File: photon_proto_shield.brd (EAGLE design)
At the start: 35.6 x 35.6 mm, 15 parts

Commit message: update
changed name on silk
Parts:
- added LOGO1: SFE_LOGO_NAME.1_INCH, SparkFun-Aesthetics:SFE_LOGO_NAME_.1
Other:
- board text added: "PROTO SHIELD FOR PHOTON"
- board text removed: "PHOTON PROTO SHIELD"
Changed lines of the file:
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@@
 <layer number="47" name="Measures" color="7" fill="1" visible="no" active="yes"/>
 <layer number="48" name="Document" color="7" fill="1" visible="no" active="yes"/>
-<layer number="49" name="Reference" color="7" fill="1" visible="yes" active="yes"/>
+<layer number="49" name="Reference" color="7" fill="1" visible="no" active="yes"/>
 <layer number="50" name="dxf" color="7" fill="1" visible="no" active="no"/>
 <layer number="51" name="tDocu" color="6" fill="1" visible="yes" active="yes"/>
@@
 <wire x1="33.02" y1="0" x2="2.54" y2="0" width="0.2032" layer="20"/>
 <wire x1="2.54" y1="0" x2="0" y2="2.54" width="0.2032" layer="20" curve="-90"/>
-<text x="35.052" y="6.858" size="1.143" layer="21" font="vector" ratio="15" rot="R90">PHOTON PROTO SHIELD</text>
+<text x="34.925" y="4.826" size="1.016" layer="21" font="vector" ratio="15" rot="R90">PROTO SHIELD FOR PHOTON</text>
 <text x="15.494" y="32.004" size="0.8128" layer="21" font="vector" ratio="15">3V3</text>
 <text x="18.161" y="32.004" size="0.8128" layer="21" font="vector" ratio="15">SDA</text>
@@
 <dimension x1="0" y1="0" x2="0" y2="35.56" x3="-7.62" y3="17.78" textsize="0.8128" textratio="15" layer="47" unit="inch"/>
 <dimension x1="35.56" y1="35.56" x2="30.734" y2="33.02" x3="33.147" y3="36.83" textsize="0.8128" textratio="15" layer="47" dtype="horizontal" unit="inch"/>
-<text x="33.909" y="6.858" size="1.143" layer="22" font="vector" ratio="15" rot="MR90">PHOTON PROTO SHIELD</text>
+<text x="33.909" y="4.826" size="1.016" layer="22" font="vector" ratio="15" rot="MR90">PROTO SHIELD FOR PHOTON</text>
 <text x="15.113" y="27.94" size="1.016" layer="22" font="vector" ratio="15" rot="MR0">GND</text>
 <text x="22.86" y="27.94" size="1.016" layer="22" font="vector" ratio="15" rot="MR0">3V3</text>
@@
 <element name="JP9" library="SparkFun-Connectors" package="1X09_NO_SILK" value="" x="21.59" y="6.35" rot="R90"/>
 <element name="JP10" library="SparkFun-Connectors" package="1X09_NO_SILK" value="" x="24.13" y="6.35" rot="R90"/>
+<element name="LOGO1" library="SparkFun-Aesthetics" package="SFE_LOGO_NAME_.1" value="SFE_LOGO_NAME.1_INCH" x="0" y="5.461" rot="MR90"/>
 </elements>
 <signals>

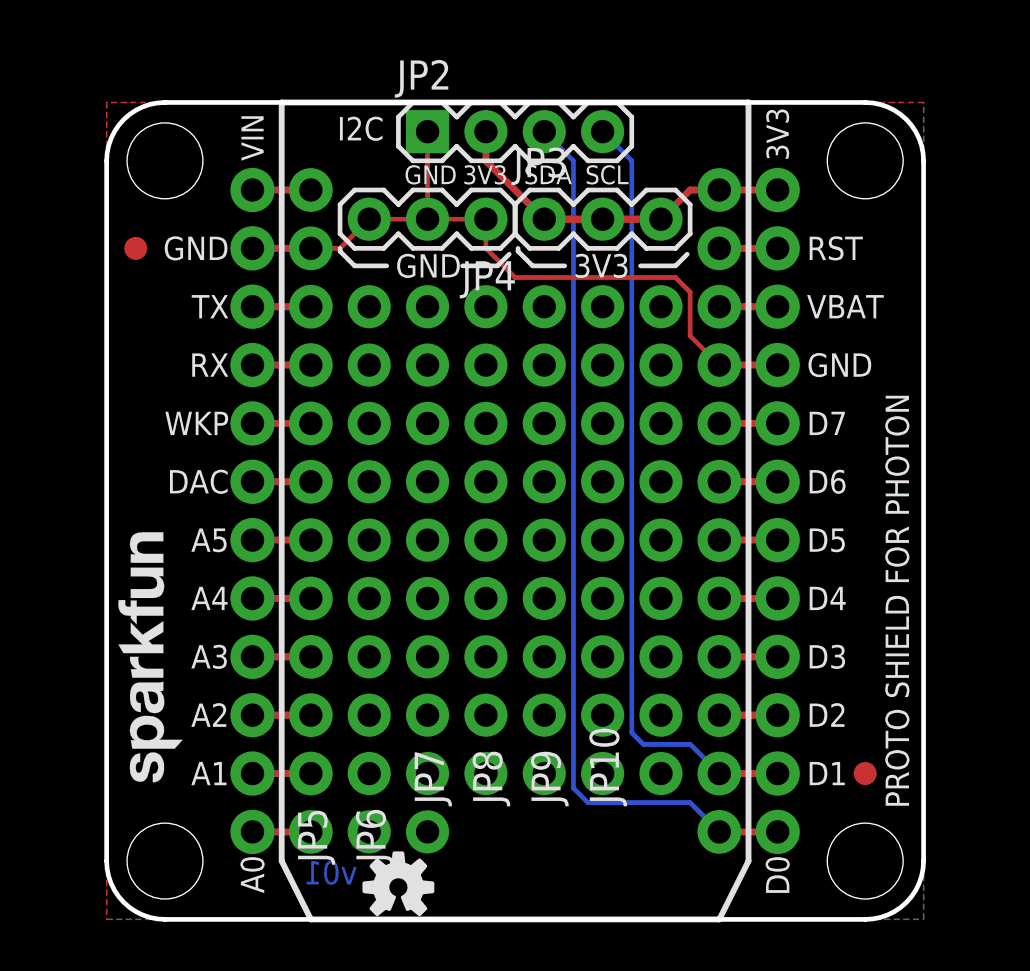
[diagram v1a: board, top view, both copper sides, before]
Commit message: Adding gap between Photon and pin breakouts.
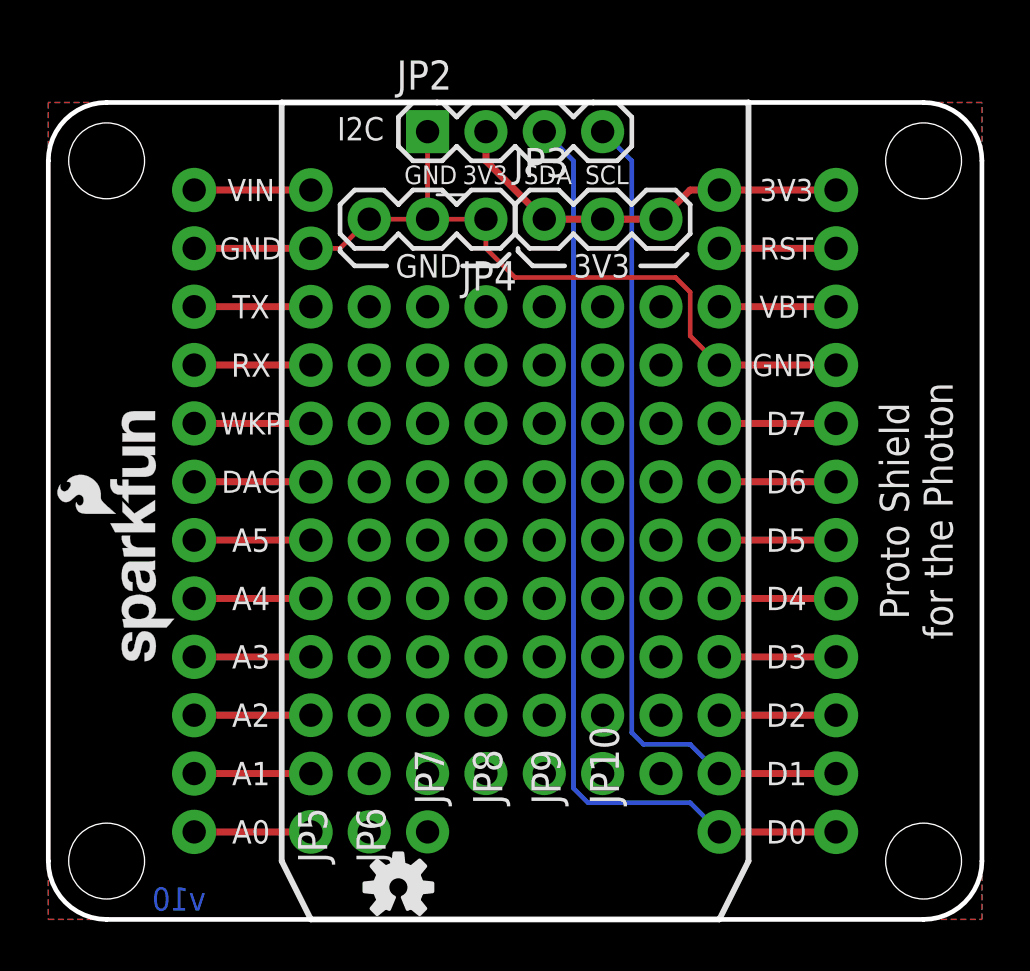
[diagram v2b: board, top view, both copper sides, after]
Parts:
- removed FID1, FID2: FIDUCIAL1X2, SparkFun-Aesthetics:FIDUCIAL-1X2
- JP1: value SPARK_PHOTONTEMPLATE -> SPARK_PHOTONTEMPLATE_WIDE; device template_temp:SPARK_PHOTON_TEMPLATE -> template_temp:SPARK_PHOTON_TEMPLATE_WIDE
- LOGO1, LOGO3: value SFE_LOGO_NAME.1_INCH -> SFE_LOGO_NAME_FLAME.1_INCH; device SparkFun-Aesthetics:SFE_LOGO_NAME_.1 -> SparkFun-Aesthetics:SFE_LOGO_NAME_FLAME_.1
- moved LOGO3 17.2 mm to (3.05, 22.6), flipped to the bottom, turned to 270 degrees
- moved LOGO1 6.14 mm to (3.05, 10.8), flipped to the top
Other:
- board size 35.6 x 35.6 mm -> 40.6 x 35.6 mm
- board text added: "Proto Shield for the Photon"
- board text added: "v10"
- board text removed: "PROTO SHIELD FOR PHOTON"
- board text removed: "v01"
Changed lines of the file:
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@@
 <board>
 <plain>
-<wire x1="0" y1="2.54" x2="0" y2="33.02" width="0.2032" layer="20"/>
-<wire x1="0" y1="33.02" x2="2.54" y2="35.56" width="0.2032" layer="20" curve="-90"/>
-<wire x1="2.54" y1="35.56" x2="33.02" y2="35.56" width="0.2032" layer="20"/>
-<wire x1="33.02" y1="35.56" x2="35.56" y2="33.02" width="0.2032" layer="20" curve="-90"/>
-<wire x1="35.56" y1="33.02" x2="35.56" y2="2.54" width="0.2032" layer="20"/>
-<wire x1="35.56" y1="2.54" x2="33.02" y2="0" width="0.2032" layer="20" curve="-90"/>
-<wire x1="33.02" y1="0" x2="2.54" y2="0" width="0.2032" layer="20"/>
-<wire x1="2.54" y1="0" x2="0" y2="2.54" width="0.2032" layer="20" curve="-90"/>
-<text x="34.925" y="4.826" size="1.016" layer="21" font="vector" ratio="15" rot="R90">PROTO SHIELD FOR PHOTON</text>
+<wire x1="-2.54" y1="2.54" x2="-2.54" y2="33.02" width="0.2032" layer="20"/>
+<wire x1="-2.54" y1="33.02" x2="0" y2="35.56" width="0.2032" layer="20" curve="-90"/>
+<wire x1="0" y1="35.56" x2="35.56" y2="35.56" width="0.2032" layer="20"/>
+<wire x1="35.56" y1="35.56" x2="38.1" y2="33.02" width="0.2032" layer="20" curve="-90"/>
+<wire x1="38.1" y1="33.02" x2="38.1" y2="2.54" width="0.2032" layer="20"/>
+<wire x1="38.1" y1="2.54" x2="35.56" y2="0" width="0.2032" layer="20" curve="-90"/>
+<wire x1="35.56" y1="0" x2="0" y2="0" width="0.2032" layer="20"/>
+<wire x1="0" y1="0" x2="-2.54" y2="2.54" width="0.2032" layer="20" curve="-90"/>
+<text x="36.83" y="17.78" size="1.27" layer="21" font="vector" ratio="15" rot="R90" align="bottom-center">Proto Shield
+for the Photon</text>
 <text x="15.494" y="32.004" size="0.8128" layer="21" font="vector" ratio="15">3V3</text>
 <text x="18.161" y="32.004" size="0.8128" layer="21" font="vector" ratio="15">SDA</text>
@@
 <dimension x1="0" y1="0" x2="0" y2="35.56" x3="-7.62" y3="17.78" textsize="0.8128" textratio="15" layer="47" unit="inch"/>
 <dimension x1="35.56" y1="35.56" x2="30.734" y2="33.02" x3="33.147" y3="36.83" textsize="0.8128" textratio="15" layer="47" dtype="horizontal" unit="inch"/>
-<text x="33.909" y="4.826" size="1.016" layer="22" font="vector" ratio="15" rot="MR90">PROTO SHIELD FOR PHOTON</text>
 <text x="15.113" y="27.94" size="1.016" layer="22" font="vector" ratio="15" rot="MR0">GND</text>
 <text x="22.86" y="27.94" size="1.016" layer="22" font="vector" ratio="15" rot="MR0">3V3</text>
 <text x="10.033" y="33.909" size="1.016" layer="21" font="vector" ratio="15">I2C</text>
-<text x="10.922" y="1.524" size="1.016" layer="16" font="vector" ratio="23" rot="MR0">v01</text>
+<text x="4.318" y="0.381" size="1.016" layer="16" font="vector" ratio="15" rot="MR0">v10</text>
 <wire x1="15.494" y1="28.448" x2="17.018" y2="28.448" width="0.2032" layer="21"/>
 <wire x1="17.018" y1="28.448" x2="17.526" y2="28.956" width="0.2032" layer="21"/>
@@
 <text x="12.192" y="33.909" size="1.016" layer="22" font="vector" ratio="15" rot="MR0">I2C</text>
 <text x="19.05" y="-12.7" size="1.778" layer="51" font="vector" ratio="10">Ben Leduc-Mills</text>
+<text x="36.83" y="17.78" size="1.27" layer="22" font="vector" ratio="15" rot="MR270" align="bottom-center">Proto Shield
+for the Photon</text>
 </plain>
 <attributes>
@@
 <elements>
 <element name="FRAME1" library="SparkFun-Aesthetics" package="CREATIVE_COMMONS" value="" x="-11.43" y="-12.7">
-<attribute name="VERSION" value="v01" x="-11.43" y="-12.7" size="1.778" layer="27" display="off"/>
+<attribute name="VERSION" value="v10" x="-11.43" y="-12.7" size="1.778" layer="27" display="off"/>
 <attribute name="DESIGNER" value="Ben Leduc-Mills" x="-11.43" y="-12.7" size="1.778" layer="27" display="off"/>
 </element>
-<element name="JP1" library="template_temp" package="SPARK_PHOTON_TEMPLATE" value="SPARK_PHOTONTEMPLATE" x="7.62" y="0"/>
+<element name="JP1" library="template_temp" package="SPARK_PHOTON_TEMPLATE_WIDE" value="SPARK_PHOTONTEMPLATE_WIDE" x="7.62" y="0"/>
 <element name="LOGO2" library="SparkFun-Aesthetics" package="OSHW-LOGO-S" value="OSHW-LOGOS" x="12.7" y="1.397"/>
-<element name="LOGO3" library="SparkFun-Aesthetics" package="SFE_LOGO_NAME_.1" value="SFE_LOGO_NAME.1_INCH" x="3.81" y="5.461" rot="R90"/>
-<element name="FID1" library="SparkFun-Aesthetics" package="FIDUCIAL-1X2" value="FIDUCIAL1X2" x="1.27" y="29.21"/>
-<element name="FID2" library="SparkFun-Aesthetics" package="FIDUCIAL-1X2" value="FIDUCIAL1X2" x="33.02" y="6.35"/>
 <element name="JP2" library="SparkFun-Connectors" package="1X04" value="" x="13.97" y="34.29"/>
 <element name="JP3" library="SparkFun-Connectors" package="1X03" value="" x="19.05" y="30.48"/>
@@
 <element name="JP9" library="SparkFun-Connectors" package="1X09_NO_SILK" value="" x="21.59" y="6.35" rot="R90"/>
 <element name="JP10" library="SparkFun-Connectors" package="1X09_NO_SILK" value="" x="24.13" y="6.35" rot="R90"/>
-<element name="LOGO1" library="SparkFun-Aesthetics" package="SFE_LOGO_NAME_.1" value="SFE_LOGO_NAME.1_INCH" x="0" y="5.461" rot="MR90"/>
+<element name="LOGO1" library="SparkFun-Aesthetics" package="SFE_LOGO_NAME_FLAME_.1" value="SFE_LOGO_NAME_FLAME.1_INCH" x="3.048" y="10.795" rot="R90"/>
+<element name="LOGO3" library="SparkFun-Aesthetics" package="SFE_LOGO_NAME_FLAME_.1" value="SFE_LOGO_NAME_FLAME.1_INCH" x="3.048" y="22.606" rot="MR270"/>
 </elements>
 <signals>
@@
 <contactref element="JP1" pad="21"/>
 <polygon width="0.254" layer="1" isolate="0.3048">
-<vertex x="0" y="35.56"/>
-<vertex x="0" y="0"/>
-<vertex x="35.56" y="0"/>
-<vertex x="35.56" y="35.56"/>
+<vertex x="-2.54" y="35.56"/>
+<vertex x="-2.54" y="0"/>
+<vertex x="38.1" y="0"/>
+<vertex x="38.1" y="35.56"/>
 </polygon>
 <polygon width="0.254" layer="16" isolate="0.3048">
-<vertex x="0" y="35.56"/>
-<vertex x="0" y="0"/>
-<vertex x="35.56" y="0"/>
-<vertex x="35.56" y="35.56"/>
+<vertex x="-2.54" y="35.56"/>
+<vertex x="-2.54" y="0"/>
+<vertex x="38.1" y="0"/>
+<vertex x="38.1" y="35.56"/>
 </polygon>
 <contactref element="JP1" pad="GND@2"/>
